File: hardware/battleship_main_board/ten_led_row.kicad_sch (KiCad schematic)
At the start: 10 parts

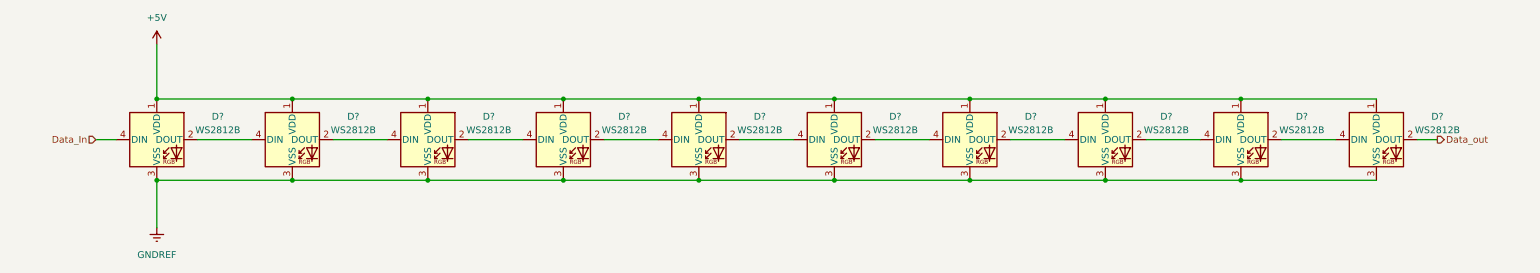
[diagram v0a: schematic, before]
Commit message: Got schematic to place that can be turned into a ratsnest
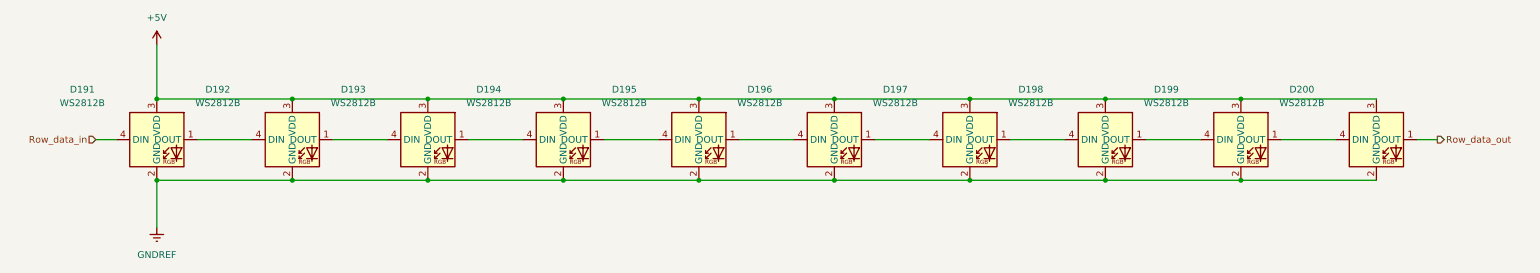
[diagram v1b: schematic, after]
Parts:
- D191, D192, D193, D194, D195, D196, D197, D198, D199, D200: renamed from D?; footprint LED_SMD:LED_WS2812B_PLCC4_5.0x5.0mm_P3.2mm -> LED_THT:LED_D5.0mm-4_RGB; symbol LED:WS2812B -> Battleship:WS2812B_THT_LED
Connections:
- net Data_out is gone; now on net GNDREF: D200.2 (GND)
- net +5V: now also D191.3 (VDD), D192.3 (VDD), D193.3 (VDD), D194.3 (VDD), D195.3 (VDD), D196.3 (VDD), D197.3 (VDD), D198.3 (VDD), D199.3 (VDD), D200.3 (VDD); no longer D191.1 (VDD), D192.1 (VDD), D193.1 (VDD), D194.1 (VDD), D195.1 (VDD), D196.1 (VDD), D197.1 (VDD), D198.1 (VDD), D199.1 (VDD), D200.1 (VDD)
- net GNDREF: now also D191.2 (GND), D192.2 (GND), D193.2 (GND), D194.2 (GND), D195.2 (GND), D196.2 (GND), D197.2 (GND), D198.2 (GND), D199.2 (GND); no longer D191.3 (VSS), D192.3 (VSS), D193.3 (VSS), D194.3 (VSS), D195.3 (VSS), D196.3 (VSS), D197.3 (VSS), D198.3 (VSS), D199.3 (VSS), D200.3 (VSS)
- net at D196.4 (DIN): now also D195.1 (DOUT); no longer D195.2 (DOUT)
- net at D195.4 (DIN): now also D194.1 (DOUT); no longer D194.2 (DOUT)
- net at D198.4 (DIN): now also D197.1 (DOUT); no longer D197.2 (DOUT)
- net at D197.4 (DIN): now also D196.1 (DOUT); no longer D196.2 (DOUT)
- net at D193.4 (DIN): now also D192.1 (DOUT); no longer D192.2 (DOUT)
- net at D192.4 (DIN): now also D191.1 (DOUT); no longer D191.2 (DOUT)
- net at D200.4 (DIN): now also D199.1 (DOUT); no longer D199.2 (DOUT)
- net at D194.4 (DIN): now also D193.1 (DOUT); no longer D193.2 (DOUT)
- net at D199.4 (DIN): now also D198.1 (DOUT); no longer D198.2 (DOUT)
- net Data_In renamed Row_data_in
- new net Row_data_out: D200.1 (DOUT)

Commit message: Fixed annotations so that button rows are in order
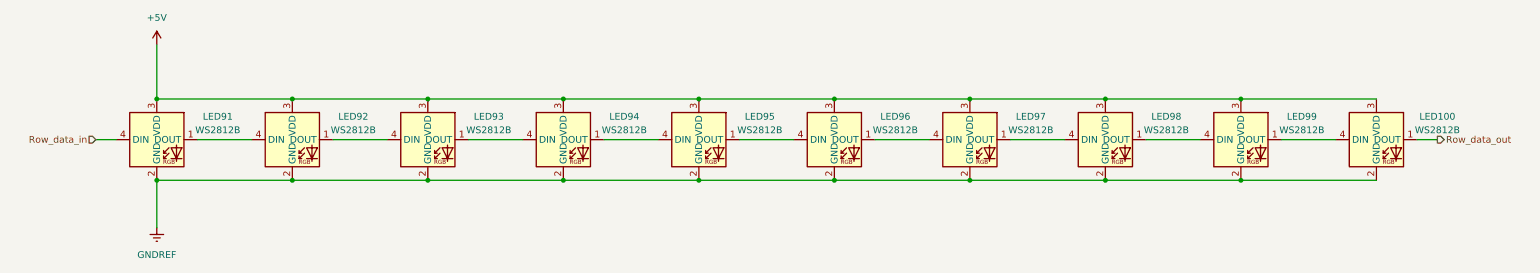
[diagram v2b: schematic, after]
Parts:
- renumbered D200 to LED100, D191 to LED91, D192 to LED92, D193 to LED93, D194 to LED94, D195 to LED95, D196 to LED96, D197 to LED97, D198 to LED98, D199 to LED99
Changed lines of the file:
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@@
   (symbol (lib_id "Battleship:WS2812B_THT_LED") (at 110.49 62.23 0)
     (in_bom yes) (on_board yes) (fields_autoplaced)
-    (property "Reference" "D195" (id 0) (at 121.92 57.8993 0))
-    (property "Value" "WS2812B" (id 1) (at 121.92 60.4393 0))
+    (property "Reference" "LED95" (id 0) (at 147.32 62.9793 0))
+    (property "Value" "WS2812B" (id 1) (at 147.32 65.5193 0))
     (property "Footprint" "LED_THT:LED_D5.0mm-4_RGB" (id 2) (at 125.73 48.26 0)
       (effects (font (size 1.27 1.27)) hide)
@@
   (symbol (lib_id "Battleship:WS2812B_THT_LED") (at 161.29 62.23 0)
     (in_bom yes) (on_board yes) (fields_autoplaced)
-    (property "Reference" "D197" (id 0) (at 172.72 57.8993 0))
-    (property "Value" "WS2812B" (id 1) (at 172.72 60.4393 0))
+    (property "Reference" "LED97" (id 0) (at 198.12 62.9793 0))
+    (property "Value" "WS2812B" (id 1) (at 198.12 65.5193 0))
     (property "Footprint" "LED_THT:LED_D5.0mm-4_RGB" (id 2) (at 176.53 48.26 0)
       (effects (font (size 1.27 1.27)) hide)
@@
   (symbol (lib_id "Battleship:WS2812B_THT_LED") (at 34.29 62.23 0)
     (in_bom yes) (on_board yes) (fields_autoplaced)
-    (property "Reference" "D192" (id 0) (at 45.72 57.8993 0))
-    (property "Value" "WS2812B" (id 1) (at 45.72 60.4393 0))
+    (property "Reference" "LED92" (id 0) (at 71.12 62.9793 0))
+    (property "Value" "WS2812B" (id 1) (at 71.12 65.5193 0))
     (property "Footprint" "LED_THT:LED_D5.0mm-4_RGB" (id 2) (at 49.53 48.26 0)
       (effects (font (size 1.27 1.27)) hide)
@@
   (symbol (lib_id "Battleship:WS2812B_THT_LED") (at 8.89 62.23 0)
     (in_bom yes) (on_board yes) (fields_autoplaced)
-    (property "Reference" "D191" (id 0) (at 20.32 57.8993 0))
-    (property "Value" "WS2812B" (id 1) (at 20.32 60.4393 0))
+    (property "Reference" "LED91" (id 0) (at 45.72 62.9793 0))
+    (property "Value" "WS2812B" (id 1) (at 45.72 65.5193 0))
     (property "Footprint" "LED_THT:LED_D5.0mm-4_RGB" (id 2) (at 24.13 48.26 0)
       (effects (font (size 1.27 1.27)) hide)
@@
   (symbol (lib_id "Battleship:WS2812B_THT_LED") (at 135.89 62.23 0)
     (in_bom yes) (on_board yes) (fields_autoplaced)
-    (property "Reference" "D196" (id 0) (at 147.32 57.8993 0))
-    (property "Value" "WS2812B" (id 1) (at 147.32 60.4393 0))
+    (property "Reference" "LED96" (id 0) (at 172.72 62.9793 0))
+    (property "Value" "WS2812B" (id 1) (at 172.72 65.5193 0))
     (property "Footprint" "LED_THT:LED_D5.0mm-4_RGB" (id 2) (at 151.13 48.26 0)
       (effects (font (size 1.27 1.27)) hide)
@@
   (symbol (lib_id "power:GNDREF") (at 34.29 83.82 0)
     (in_bom yes) (on_board yes) (fields_autoplaced)
-    (property "Reference" "#PWR040" (id 0) (at 34.29 90.17 0)
+    (property "Reference" "#PWR020" (id 0) (at 34.29 90.17 0)
       (effects (font (size 1.27 1.27)) hide)
     )
@@
   (symbol (lib_id "power:+5V") (at 34.29 49.53 0)
     (in_bom yes) (on_board yes) (fields_autoplaced)
-    (property "Reference" "#PWR039" (id 0) (at 34.29 53.34 0)
+    (property "Reference" "#PWR019" (id 0) (at 34.29 53.34 0)
       (effects (font (size 1.27 1.27)) hide)
     )
@@
   (symbol (lib_id "Battleship:WS2812B_THT_LED") (at 237.49 62.23 0)
     (in_bom yes) (on_board yes) (fields_autoplaced)
-    (property "Reference" "D200" (id 0) (at 248.92 57.8993 0))
-    (property "Value" "WS2812B" (id 1) (at 248.92 60.4393 0))
+    (property "Reference" "LED100" (id 0) (at 274.32 62.9793 0))
+    (property "Value" "WS2812B" (id 1) (at 274.32 65.5193 0))
     (property "Footprint" "LED_THT:LED_D5.0mm-4_RGB" (id 2) (at 252.73 48.26 0)
       (effects (font (size 1.27 1.27)) hide)
@@
   (symbol (lib_id "Battleship:WS2812B_THT_LED") (at 59.69 62.23 0)
     (in_bom yes) (on_board yes) (fields_autoplaced)
-    (property "Reference" "D193" (id 0) (at 71.12 57.8993 0))
-    (property "Value" "WS2812B" (id 1) (at 71.12 60.4393 0))
+    (property "Reference" "LED93" (id 0) (at 96.52 62.9793 0))
+    (property "Value" "WS2812B" (id 1) (at 96.52 65.5193 0))
     (property "Footprint" "LED_THT:LED_D5.0mm-4_RGB" (id 2) (at 74.93 48.26 0)
       (effects (font (size 1.27 1.27)) hide)
@@
   (symbol (lib_id "Battleship:WS2812B_THT_LED") (at 212.09 62.23 0)
     (in_bom yes) (on_board yes) (fields_autoplaced)
-    (property "Reference" "D199" (id 0) (at 223.52 57.8993 0))
-    (property "Value" "WS2812B" (id 1) (at 223.52 60.4393 0))
+    (property "Reference" "LED99" (id 0) (at 248.92 62.9793 0))
+    (property "Value" "WS2812B" (id 1) (at 248.92 65.5193 0))
     (property "Footprint" "LED_THT:LED_D5.0mm-4_RGB" (id 2) (at 227.33 48.26 0)
       (effects (font (size 1.27 1.27)) hide)
@@
   (symbol (lib_id "Battleship:WS2812B_THT_LED") (at 186.69 62.23 0)
     (in_bom yes) (on_board yes) (fields_autoplaced)
-    (property "Reference" "D198" (id 0) (at 198.12 57.8993 0))
-    (property "Value" "WS2812B" (id 1) (at 198.12 60.4393 0))
+    (property "Reference" "LED98" (id 0) (at 223.52 62.9793 0))
+    (property "Value" "WS2812B" (id 1) (at 223.52 65.5193 0))
     (property "Footprint" "LED_THT:LED_D5.0mm-4_RGB" (id 2) (at 201.93 48.26 0)
       (effects (font (size 1.27 1.27)) hide)
@@
   (symbol (lib_id "Battleship:WS2812B_THT_LED") (at 85.09 62.23 0)
     (in_bom yes) (on_board yes) (fields_autoplaced)
-    (property "Reference" "D194" (id 0) (at 96.52 57.8993 0))
-    (property "Value" "WS2812B" (id 1) (at 96.52 60.4393 0))
+    (property "Reference" "LED94" (id 0) (at 121.92 62.9793 0))
+    (property "Value" "WS2812B" (id 1) (at 121.92 65.5193 0))
     (property "Footprint" "LED_THT:LED_D5.0mm-4_RGB" (id 2) (at 100.33 48.26 0)
       (effects (font (size 1.27 1.27)) hide)
